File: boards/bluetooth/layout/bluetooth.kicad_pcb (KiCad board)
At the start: 2 copper layers, 16 x 25 mm, 9 parts, among them U1 HM-19

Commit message: 🐛 Identify the Bluetooth module on CC and pull its RESETB up
M6: the plug's CC1 and CC2 join its D+ contacts. The main board's UART4 TX
idles high and pulls its CC contacts (5.1 kOhm Rd each) to about 3.2 V
through them, a level no USB Type-C source makes across a sink's Rd (R2.0
Tables 4-35, 4-36: 2.18 / 2.04 V max), so the main board can switch 3V3
onto SBU only for the module and leave SBU open for every USB partner.

m17: R4 10 kOhm from HM-19 RESETB to 3V3; the CC2640R2F's RESET_N has no
internal pull-up (SWRS204C Table 7-1).

The board's minimum silkscreen text height is 0.5 mm, the size of its
reference designators. The layout gets the packages' new courtyards and R4,
not yet placed.
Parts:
- added R4: 10k 1% 100mW, stdlib_kicad-footprints_Resistor_SMD:R_0603_1608Metric, F.Cu at (158.0, 116.8)
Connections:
- U1 pad 11: U1.NC_HM19_RESETB -> RESETB
- USB1 pad 11: USB1.NC_PLUG_CC2 -> UART_RX
- USB1 pad 3: USB1.NC_PLUG_CC1 -> UART_RX

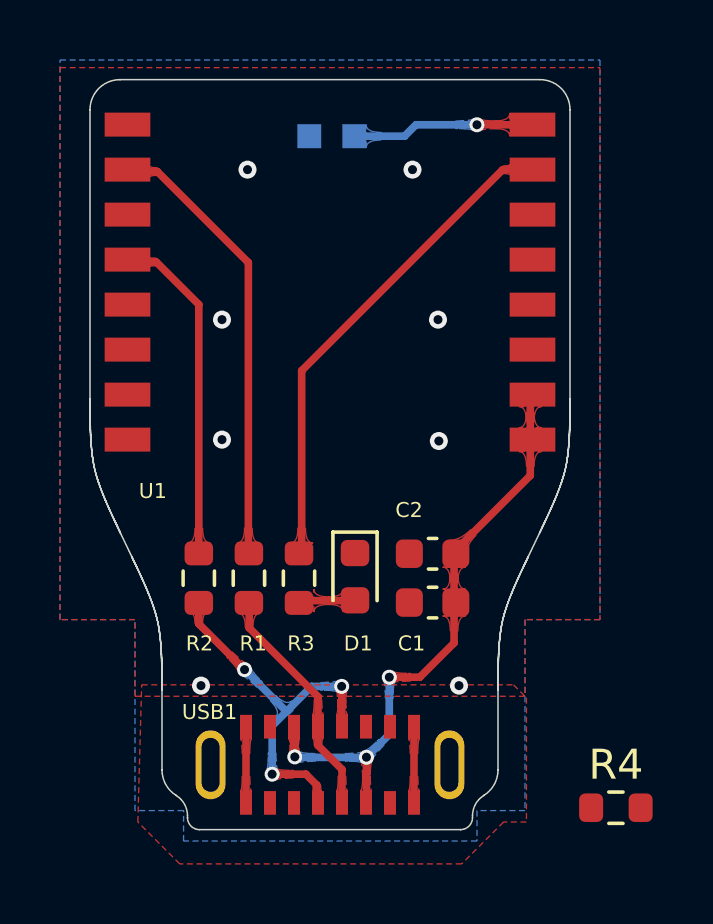
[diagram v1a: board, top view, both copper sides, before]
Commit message: ✨ Place and route the Bluetooth module's review fixes
boards/bluetooth/layout/fixes.py, a one-off pcbnew script:
- removes the seven 1-12 nm Edge.Cuts lines of the Altium conversion and
  joins their neighbours, so the outline closes (invalid_outline);
- joins USB1's CC1 and CC2 pads to the adjacent D+ pads (the signature);
- places R4 between the HM-19 and C2, to C2's 3V3 pad and under the module
  to U1 pad 11 (RESETB), and moves C2's reference beside C2;
- refills the pours.

DRC is clean.
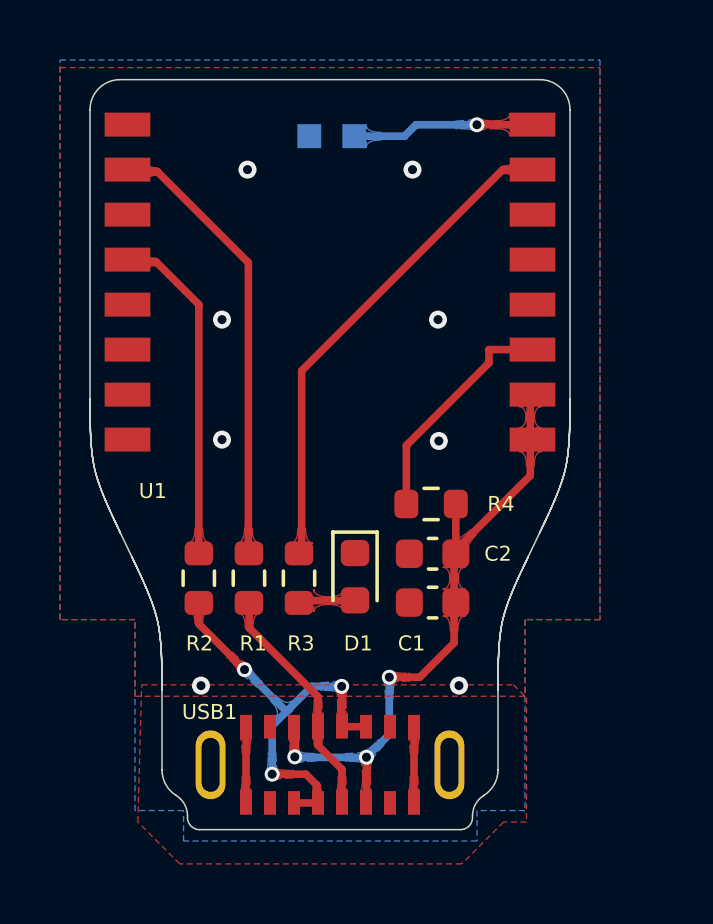
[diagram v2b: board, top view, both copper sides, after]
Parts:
- moved R4 11.9 mm to (151.9, 106.7)
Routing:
- net RESETB: track 0.00 -> 7.74 mm
- net 3V3: track 19.9 -> 21.6 mm
- net UART_RX: track 13.0 -> 14.6 mm
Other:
- outline, holes or cut-outs redrawn
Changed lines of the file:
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@@
 	(footprint "stdlib_kicad-footprints_Resistor_SMD:R_0603_1608Metric"
 		(layer "F.Cu")
-		(at 158.031105 116.773595)
+		(at 151.87112 106.65)
 		(descr "Resistor SMD 0603 (1608 Metric), square (rectangular) end terminal, IPC-7351 nominal, (Body size source: IPC-SM-782 page 72, https://www.pcb-3d.com/wordpress/wp-content/uploads/ipc-sm-782a_amendment_1_and_2.pdf)")
 		(tags "resistor")
 		(property "Reference" "R4"
-			(at 0 -1.43 0)
+			(at 2.32888 0 0)
+			(unlocked yes)
 			(layer "F.SilkS")
 			(effects
 				(font
-					(size 1 1)
-					(thickness 0.15)
+					(size 0.5 0.5)
+					(thickness 0.154)
 				)
 			)
@@
 		(tags "capacitor")
 		(property "Reference" "C2"
-			(at -0.78646 -1.45437 0)
+			(at 2.17888 0.002365 0)
 			(unlocked yes)
 			(layer "F.SilkS")
@@
 	(gr_line
 		(start 141.501094 92.503595)
-		(end 141.501095 92.503595)
-		(stroke
-			(width 0.05)
-			(type solid)
-		)
-		(layer "Edge.Cuts")
-	)
-	(gr_line
-		(start 141.501095 92.503595)
 		(end 155.501105 92.503595)
 		(stroke
@@
 	)
 	(gr_line
-		(start 142.901095 115.514905)
-		(end 142.901095 112.847575)
-		(stroke
-			(width 0.05)
-			(type solid)
-		)
-		(layer "Edge.Cuts")
-	)
-	(gr_line
 		(start 142.901095 115.514906)
-		(end 142.901095 115.514905)
+		(end 142.901095 112.847575)
 		(stroke
 			(width 0.05)
@@
 		(layer "Edge.Cuts")
 	)
-	(gr_line
-		(start 143.373319 116.36429)
-		(end 143.373321 116.36429)
-		(stroke
-			(width 0.05)
-			(type solid)
-		)
-		(layer "Edge.Cuts")
-	)
 	(gr_arc
-		(start 143.373319 116.36429)
+		(start 143.373321 116.36429)
 		(mid 143.65032 116.655062)
 		(end 143.751095 117.043797)
@@
 	(gr_line
 		(start 143.751095 117.103595)
-		(end 143.751105 117.103595)
-		(stroke
-			(width 0.05)
-			(type solid)
-		)
-		(layer "Edge.Cuts")
-	)
-	(gr_line
-		(start 143.751105 117.103595)
 		(end 143.751095 117.043797)
 		(stroke
@@
 	)
 	(gr_line
-		(start 152.851095 117.503595)
-		(end 144.151095 117.503595)
-		(stroke
-			(width 0.05)
-			(type solid)
-		)
-		(layer "Edge.Cuts")
-	)
-	(gr_line
 		(start 152.851094 117.503595)
-		(end 152.851095 117.503595)
-		(stroke
-			(width 0.05)
-			(type solid)
-		)
-		(layer "Edge.Cuts")
-	)
-	(gr_line
-		(start 153.251095 117.043795)
-		(end 153.251095 117.103596)
+		(end 144.151095 117.503595)
 		(stroke
 			(width 0.05)
@@
 	(gr_line
 		(start 153.251105 117.043798)
-		(end 153.251095 117.043795)
+		(end 153.251095 117.103596)
 		(stroke
 			(width 0.05)
@@
 	)
 	(gr_line
-		(start 153.628876 116.36429)
-		(end 153.628885 116.364298)
-		(stroke
-			(width 0.05)
-			(type solid)
-		)
-		(layer "Edge.Cuts")
-	)
-	(gr_line
 		(start 154.101095 112.847575)
 		(end 154.101095 115.514907)
@@
 		(start 154.101095 115.514907)
 		(mid 153.975105 116.00082)
-		(end 153.628876 116.36429)
+		(end 153.628885 116.364298)
 		(stroke
 			(width 0.05)
@@
 	)
 	(segment
+		(start 151.04612 106.65)
+		(end 151.04612 104.7)
+		(width 0.254)
+		(layer "F.Cu")
+		(net "RESETB")
+	)
+	(segment
+		(start 153.80012 101.946)
+		(end 153.80012 101.504)
+		(width 0.254)
+		(layer "F.Cu")
+		(net "RESETB")
+	)
+	(segment
+		(start 153.80012 101.504)
+		(end 155.251095 101.503595)
+		(width 0.254)
+		(layer "F.Cu")
+		(net "RESETB")
+	)
+	(segment
+		(start 151.04612 104.7)
+		(end 153.80012 101.946)
+		(width 0.254)
+		(layer "F.Cu")
+		(net "RESETB")
+	)
+	(segment
 		(start 152.621145 108.307635)
 		(end 152.621145 108.257635)
@@
 		(net "3V3")
 	)
+	(segment
+		(start 152.69612 106.65)
+		(end 152.69612 108.307635)
+		(width 0.254)
+		(layer "F.Cu")
+		(net "3V3")
+	)
 	(via
 		(at 147.327485 115.079005)
@@
 	)
 	(segment
+		(start 149.701075 114.073615)
+		(end 148.901075 114.073615)
+		(width 0.254)
+		(layer "F.Cu")
+		(net "UART_RX")
+	)
+	(segment
 		(start 146.572075 115.655995)
 		(end 147.696455 115.655995)
@@
 		(end 148.101075 116.613615)
 		(width 0.254)
+		(layer "F.Cu")
+		(net "UART_RX")
+	)
+	(segment
+		(start 147.301075 116.613615)
+		(end 148.101075 116.613615)
+		(width 0.254)
